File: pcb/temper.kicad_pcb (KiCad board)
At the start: 6 copper layers, 164 x 234 mm, 168 parts, among them J1 ?, J2 ?, K1 ?, K2 ?, K3 ?, Q1 ?, Q2 ?, SW1 ?, SW2 ?, T1 ?, T2 ?, U1 ?, U10 ?, U11 ?, U12 ?, U13 ?, U14 ?, U15 ?, U16 ?, U17 ?, U18 ?, U19 ?, U2 ?, U20 ?, U21 ?, U22 ?, U23 ?, U24 ?, U25 ?, U26 ?, U27 ?, U3 ?, U4 ?, U5 ?, U6 ?, U7 ?, U8 ?, U9 ?

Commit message: fix(pcb): C7 to (112,206) rot180 — clears the 77mm2 C7<->K1 body interpenetration
Three at-nodes in C7's footprint block: the footprint's own (at x y angle)
and both pads' angles by delta = +90, matching what
update_footprint_positions_py produces (read out of its own output rather
than assumed). Deliberately NOT written via write_placements_to_pcb: that
path reserialises the whole board (89,908 insertions / 21,849 deletions for
this one move) into a different generator's formatting. The minimal edit is
DRC-identical to the reserialised board.

Candidate chosen from the four scored in #1471.
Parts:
- moved C7 12.0 mm to (112.0, 206.0), turned to 180 degrees
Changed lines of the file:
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@@
   )
   (footprint "Capacitor_THT:C_Rect_L18.0mm_W11.0mm_P15.00mm_FKS3_FKP3" (version 20260206) (generator kicad-footprint-generator) (layer "F.Cu")
-    (at 112 218 90)
+    (at 112 206 180)
     (descr "C, Rect series, Radial, pin pitch=15.00mm, length*width=18*11mm^2, Capacitor, http://www.wima.com/EN/WIMA_FKS_3.pdf")
     (tags "C Rect series Radial pin pitch 15.00mm length 18mm width 11mm Capacitor")
@@
       (effects (font (size 1 1) (thickness 0.15)))
     )
-    (pad "1" thru_hole circle (at 0 0 180) (size 2.4 2.4) (drill 1.2) (layers *.Cu *.Mask) (remove_unused_layers)
+    (pad "1" thru_hole circle (at 0 0 270) (size 2.4 2.4) (drill 1.2) (layers *.Cu *.Mask) (remove_unused_layers)
       (net 44 "discharge.r_snub1-p2"))
-    (pad "2" thru_hole circle (at 15 0 180) (size 2.4 2.4) (drill 1.2) (layers *.Cu *.Mask) (remove_unused_layers)
+    (pad "2" thru_hole circle (at 15 0 270) (size 2.4 2.4) (drill 1.2) (layers *.Cu *.Mask) (remove_unused_layers)
       (net 13 "PWR_RTN"))
     (model "${KICAD10_3DMODEL_DIR}/Capacitor_THT.3dshapes/C_Rect_L18.0mm_W11.0mm_P15.00mm_FKS3_FKP3.step"

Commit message: fix(safety): tie fault_any_or's spare gate inputs to GND (floating CMOS inputs) (#1502)
* fix(safety): tie fault_any_or's spare gate inputs to GND (floating CMOS inputs)

U24 (SN74HC4075, safety.fault_any_or) had its unused third-gate inputs
A3/B3/C3 on single-node nets -- floating CMOS inputs on the package that
carries the FAULT_ANY aggregation.

This is not a judgement call; it is an omission against the design's own
stated convention. All three SN74HC4075 packages have an unused third
gate. Two of them tie its inputs to GND, with comments saying why:

  fault_or3  A3/B3/C3 ~ gnd   "inputs tied GND rather than left floating
                               (same convention as fault_or gate 3 below)"
  fault_or   A3/B3/C3 ~ gnd   "Unused base-OR gate has defined inputs"
  fault_any_or                 -- missing --

The same author tied fault_any_or.C2 to GND four lines above, so the
practice was known for this exact package; the gate-3 block was simply
never written for it.

Measured on the compiled netlist before this change:

  U24 pin 11  net "a3"  nodes=1     <- floating
  U24 pin 12  net "b3"  nodes=1     <- floating
  U24 pin 13  net "c3"  nodes=1     <- floating
  U23 pins 11/12/13     net "gnd"   <- correct
  U25 pins 11/12/13     net "gnd"   <- correct

Why it matters: an unterminated HC-family input floats near the switching
threshold, biasing both output FETs partially on -- elevated ICC and a
stage that can self-oscillate and couple through the shared VCC/GND of a
package whose other two gates carry live fault signals (fault_or.Y2,
RTD_HW_FAULT, coil_thermal). The disturbance would sit directly on the
fault aggregation path.

Found by triaging the 29 single-node nets in #1500. It is also a concrete
instance of that issue's thesis: gen_schematics.py renders any single-node
pin as a KiCad `no_connect`, which is a positive assertion of deliberate
non-connection and tells ERC to stop reporting the pin. The undriven-input
check that would have caught this had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
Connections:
- U24 pad 11: a3 -> gnd
- U24 pad 12: b3 -> gnd
- U24 pad 13: c3 -> gnd

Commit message: fix(pcb): four board moves — clear the body-collision cluster and K1's isolation barrier (#1506)
* fix(pcb): move C6 -7.00mm — clears the whole 3-way body-collision cluster

C4<->C6 (14.5362mm^2), C6<->R26 (1.3200mm^2) and C22<->C6 (1.2800mm^2) are
F.Fab body interpenetrations: parts occupying the same physical space, so
the board as committed could not be assembled. Same class as the C7<->K1
overlap fixed in #1498, and the item that PR's ceiling approval listed as
"not cleared and not claimed".

C6 is the common ref in all three, so one move clears the cluster.

SEARCH, not a guess. Swept C6 over +/-12mm at 0.25mm on the rotations that
preserve its lead axis (a 26.5x7.0mm MKS4 box cap on 22.5mm pitch --
rotating it moves the leads, so rotation changes were ruled out in favour
of a pure translation), scoring every candidate with audit_body_collisions,
the same function the gate runs:

  rot  90 (current, pure translation)   687 collision-free, best 7.00mm
  rot 270 (flips end-for-end)          1497 collision-free, best 4.51mm

Took the pure translation: (66.99, 201.51) -> (59.99, 201.51), rot
unchanged at 90.

MEASURED, 5 samples per board, spread 0 in every category (STRATEGY.md
mandates median over N>=5 for any DRC-gated figure):

                        before   after   delta
  errors                   392     388      -4
  shorting_items            39      39       0
  creepage                 115     114      -1
  courtyards_overlap         6       3      -3
  unconnected items        347     347       0

Strictly better on every axis and worse on none. shorting_items -- the
fatal class on a mains board -- does not move. Connectivity does not
change, so the 7mm move breaks no routing.

ALLOWLIST PRUNED 6 -> 1. With the cluster gone, re-measuring against an
emptied allowlist (which reports every real body overlap, allowlisted or
not) leaves exactly ONE on the whole board:

  C2<->C3   115.6512 mm^2   STILL -- kept
  C5<->C7   106.8341 mm^2   GONE -- this entry's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
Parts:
- moved R56 10.2 mm to (129.2, 209.9)
- moved C6 7.00 mm to (60.0, 201.5)
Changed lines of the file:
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@@
   )
   (footprint "Capacitor_THT:C_Rect_L26.5mm_W7.0mm_P22.50mm_MKS4" (version 20260206) (generator kicad-footprint-generator) (layer "F.Cu")
-    (at 66.99 201.51 90)
+    (at 59.99 201.51 90)
     (descr "C, Rect series, Radial, pin pitch=22.50mm, length*width=26.5*7mm^2, Capacitor, http://www.wima.com/EN/WIMA_MKS_4.pdf")
     (tags "C Rect series Radial pin pitch 22.50mm length 26.5mm width 7mm Capacitor")
@@
   )
   (footprint "Resistor_SMD:R_0603_1608Metric" (version 20260206) (generator kicad-footprint-generator) (layer "F.Cu")
-    (at 119.21 207.88 90)
-    (descr "Resistor SMD 0603 (1608 Metric), square (rectangular) end terminal, IPC-7351 nominal, (Body size source: IPC-SM-782 page 72, https://www.pcb-3d.com/wordpress/wp-content/uploads/ipc-sm-782a_amendment_1_and_2.pdf)")
-    (tags "resistor")
+    (at 129.21 209.88 90)
+    (descr "Resistor SMD 0603 (1608 Metric), square (rectangular) end terminal, IPC-7351 nominal, (Body size source: IPC-SM-782 page 72, https://www.pcb-3d.com/wordpress/wp-content/uploads/ipc-sm-782a_amendment_1_and_2.pdf)")
+    (tags "resistor")

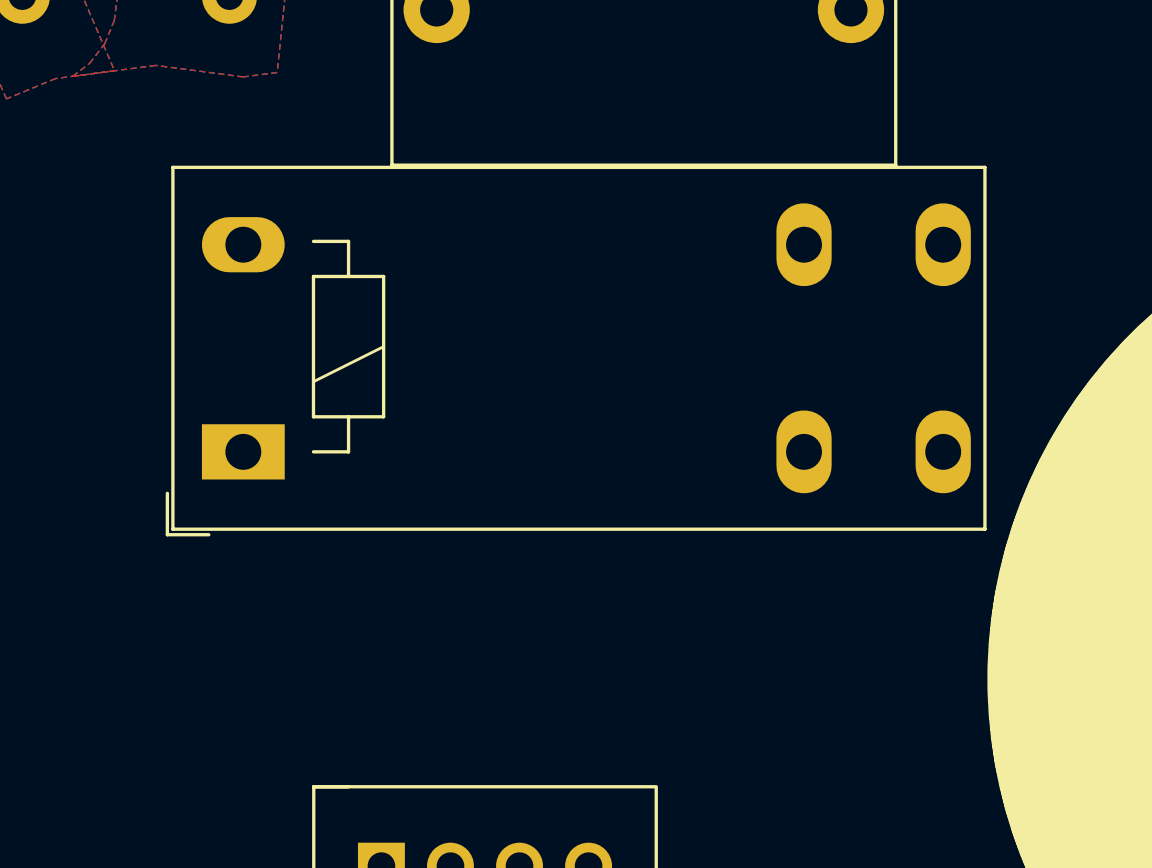
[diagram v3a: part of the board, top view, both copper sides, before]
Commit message: fix(pcb): move K1 +6.00mm — 2 of its remaining barrier findings down to 1
Follow-up to #1506, which cleared 3 of K1's 5 REQ-SAFE-01 violations
(including the pollution-degree-INDEPENDENT 6.0mm through-air breach) and
left two:

  K1<->RT1  creepage  7.000 / 12.6mm  REINFORCED
  K1<->C7   creepage  8.500 / 12.6mm  REINFORCED

#1506 originally moved RT1 and C7 to clear them and I reverted that: both
moves reintroduced kicad-cli WARNING regressions (pth_inside_courtyard
0 -> 3, silk_over_copper 46 -> 47) that would have needed an owner ceiling
raise. This commit gets most of the way there by moving K1 itself instead.

  K1 (90, 222) -> (90, 228)

WHAT I MEASURED FIRST, including the dead ends -- every candidate below was
DRC-scored, not assumed:

  RT1, 8 spread positions from 536 safety-valid candidates
    7 of 8 reintroduce pth_inside_courtyard (1-2)
    the 1 with pth=0 costs shorting_items 39 -> 42
    -> no clean RT1 move exists in that sample

  C7, 5 spread positions from 33 safety-valid candidates
    3 are clean on pth/silk/shorting, but all push kicad-cli creepage
    108 -> 109, a per-category ceiling RAISE
    -> no clean C7 move either

  K1 itself, 4 positions
    (90, 228) is clean on EVERY category -- see below
    the other 3 cost shorting_items 42-44

Moving the barrier component beat moving its neighbours. Measured on the
K1 move, 5 samples, spread 0 in every category:

                        main(post-#1506)   this PR
  REQ-SAFE-01 total            63             62
    reinforced 12.6mm inter    31             30
  kicad-cli errors            383            382
    creepage                  108            107
    courtyards_overlap          4              4
    pth_inside_courtyard        0              0
    silk_over_copper           45             45
    shorting_items             39             39
    unconnected items         347            347
  K1's own violations           2              1

Every category equal to or better. Ceiling ratch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
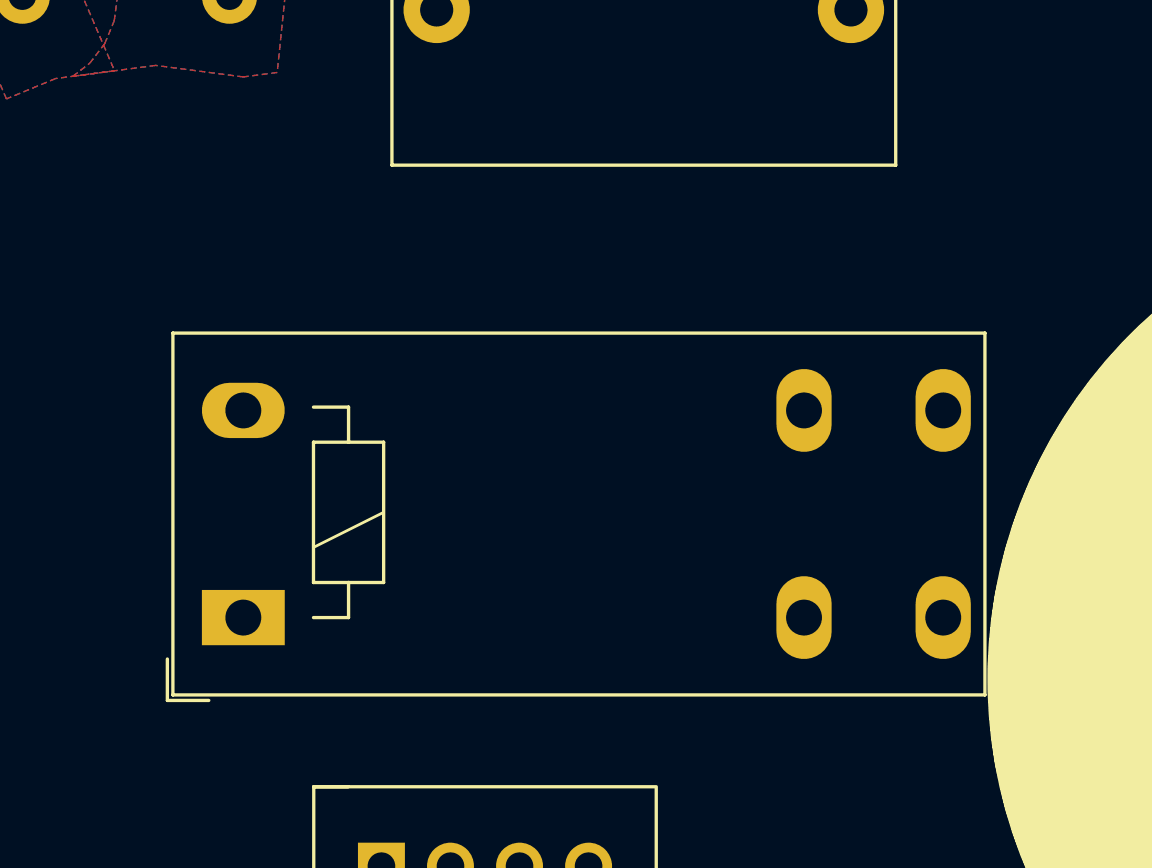
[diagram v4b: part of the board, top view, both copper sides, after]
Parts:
- moved K1 6.00 mm to (90.0, 228.0)
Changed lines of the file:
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@@
   )
   (footprint "temper:Relay_SPST_Schrack-RT33K012" (version 20231120) (generator temper-hand) (layer "F.Cu")
-    (at 90 222 0)
+    (at 90 228 0)
     (descr "TE Connectivity / Schrack Power PCB Relay RT1 Inrush, part RT33K012 (1 Form A/NO, 20A UL508/16A IEC contact, AgNi90/10 'K' contact material, 12VDC/360ohm/400mW coil). PD3 replacement for K1's incumbent Omron G4A-1A-E DC12 (8.000mm coil<->contact, measured this session with the project's canonical pad-geometry kernel -- fails the 12.6mm reinforced-creepage target). Verified 2026-07-30 (docs/evidence/2026-07-30-pd3-part-selection-k1-c6-t1.md Section 1) against TE's own 'Power PCB Relay RT1 Inrush' datasheet Rev. 0415 (https://www.enika.cz/data/files/RT3_serie.pdf), drawing ref S0418-CV: 16A/1-Form-A/pinning-5mm PCB layout. TE part 2-1393240-3; DigiKey PB2347-ND, confirmed orderable/Active this session (re-verified, not re-derived from the prior document's stock check). Contact rating: RT33K row, AgNi90/10, 20A UL508 K-version / 16A IEC general rated current, 277VAC, 4000VA breaking capacity -- matches or exceeds the outgoing G4A-1A-E's 20A/12VDC declaration on the same UL508 basis. Coil: code 012 = 12VDC, 8.4V operate, 1.2V release, 360ohm+/-10%, 400mW -- DIFFERENT from the outgoing G4A-1A-E's 160ohm/75mA/900mW coil; elec/src/modules.ato's PowerInput.r_relay_drop was retuned from 39ohm to 91ohm (Yageo RSF100JB-73-91R, same 1W axial family, re-verified orderable this session) to keep this coil at ~12.0V/33.3mA from the 15V rail (15V/(360+91)=33.26mA, 33.26mA*360ohm=11.97V, 99.8% of rated -- was 112.7% of rated with the old 39ohm dropper, above IEC 61810-1's typical 110% continuous-operation ceiling). Insulation: 'Clearance/creepage between contact and coil >=10/10mm', 'Initial dielectric strength ... 5000Vrms', Material group IIIa (same internal rating class as K2/K3's already-verified sibling RT314012, same case family). VDE Cert. No. 40007571 (same certificate already investigated in docs/evidence/2026-07-29-relay-60335-1-certification-resolution.md Track B: EN/IEC 61810-1 scope only, does not itself substitute for this board's own PCB pad-to-pad measurement -- the measurement below is what actually governs). Pad geometry (position/size/drill/shape/layers) copied verbatim from KiCad 10 stock 'Relay_THT.pretty/Relay_SPST_Schrack-RT1-16A-FormA_RM5mm.kicad_mod' (re-fetched and re-read directly this session from the local KiCad footprint library, not re-derived from the datasheet drawing a second time) -- pad-for-pad identical to the geometry docs/evidence/2026-07-30-pd3-part-selection-k1-c6-t1.md Section 1.3 already measured against this exact stock file (row pitch 7.5mm, contact sub-pitch 5.04mm, coil-to-near-contact datum span 20.3mm, overall pad-field width 22.65mm; A1 rect 3x2mm, A2 oval 3x2mm, contact pads 11/14 oval 2x3mm, each with 2 physical solder holes one per row). RENUMBERED (same convention and same reason as the sibling Relay_SPDT_Schrack-RT314012.kicad_mod file): this project's Relay_SPST atopile component (elec/src/components.ato) declares a fixed pin convention -- 1=coil1, 2=coil2, 3=NO, 4=COM -- so the stock file's native 'A1'/'A2'/'11'/'14' pad names are renamed to '1'/'2'/'3'/'4' (EN50005 pin 11=COM->renamed '4', pin 14=NO->renamed '3', matching domain_manifest.yaml's power_in.bypass_relay groups coil:['1','2'] contacts:['3','4']) so every pad resolves via scripts/resync_pcb_netlist.py's exact-match path instead of positional fallback -- this part has 6 physical pad instances (A1 x1, A2 x1, contact-11 x2, contact-14 x2) against only 4 netlist-declared pins, exactly the mismatch the RT314012 footprint's own descr already flags as a positional-fallback hazard. Pad local rotation flattened from the stock file's 180 degrees to 0, verified electrically/dimensionally identical for these axis-symmetric rect/oval pads (a 180-degree rotation of a rectangle or oval about its own centre is congruent to the unrotated shape) -- same treatment RT314012 already gave the same source file. Courtyard (29.9 x 13.6mm, -2.8,-10.55 to 27.1,3.05) and silkscreen/fab graphics copied verbatim from the stock file. GOVERNING COIL<->CONTACT SEPARATION, MEASURED this session with temper_placer.core.pin_geometry.pin_world_position + temper_placer.core.pad_geometry.pad_pair_distance (the same canonical, rotation-and-side-aware kernel PR #1146/#1152 used, NOT a datasheet-drawing hand computation): pad '1' (coil1, local (0,0), rect 3x2) <-> pad '4' (COM, local (20.3,0), oval 2x3): 17.8000mm edge-to-edge -- clears the 12.6mm PD3 reinforced-creepage target with +5.2mm margin. See docs/evidence/ for this session's full re-verification writeup. No 3D model reference carried over (same reason as RT314012: the stock file's own model points at a sibling RT2/DPDT step file, unverified for this specific part -- omitted rather than propagated).")
     (tags "relay SPST Schrack RT1 RT33K012 power relay reinforced isolation PD3")
